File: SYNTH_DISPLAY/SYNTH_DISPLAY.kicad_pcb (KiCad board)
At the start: 2 copper layers, 51.4 x 57.8 mm, 21 parts, among them CON1 AVR-ISP-6, J1 Barrel_Jack, J2 Audio-Jack-3, SW1 SW_Push_Dual, U1 L7805, U2 MSGEQ7, U3 ATTINY85-20PU

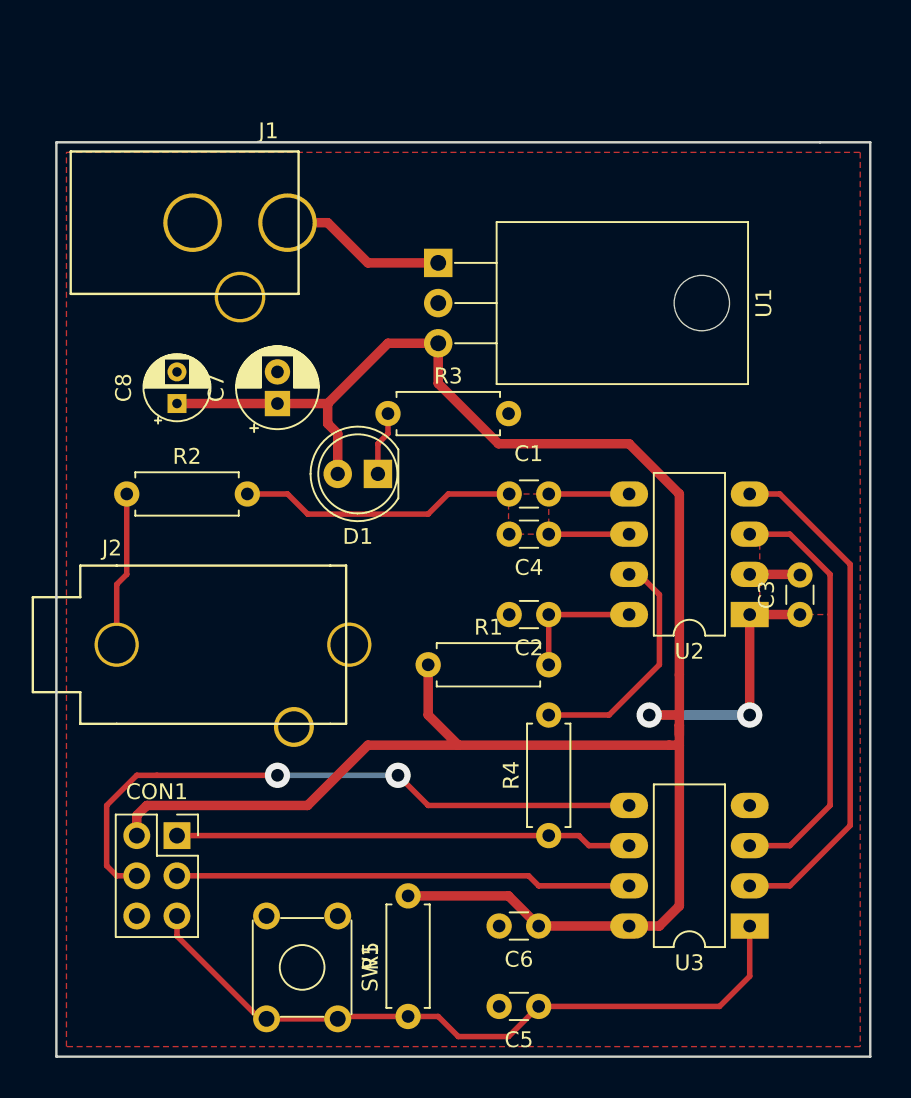
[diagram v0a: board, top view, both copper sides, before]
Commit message: added display header, mounting holes, and moved connectors
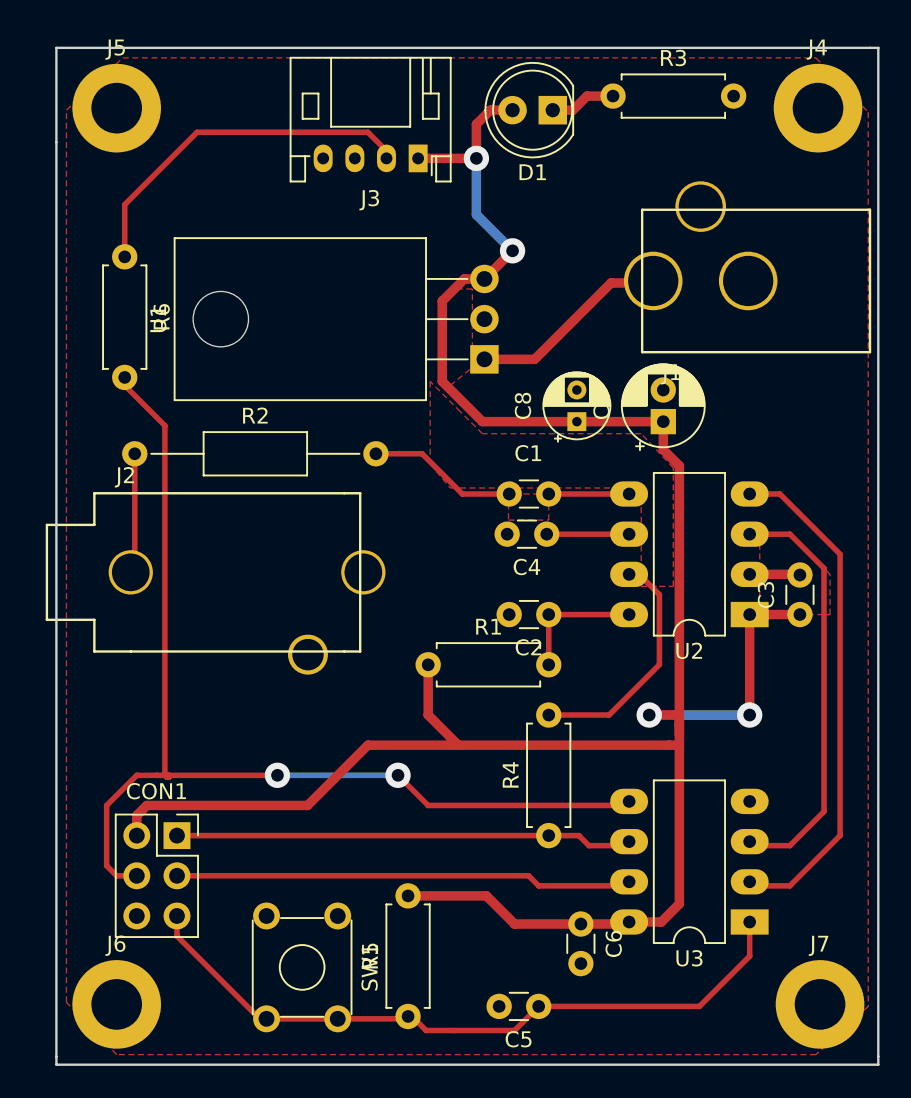
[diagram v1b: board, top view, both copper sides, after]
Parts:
- added J3: Conn_01x04, Connector_JST:JST_PH_S4B-PH-K_1x04_P2.00mm_Horizontal, F.Cu at (163.8, 64.5)
- added J4: Conn_01x01, MountingHole:MountingHole_3.2mm_M3_DIN965_Pad, F.Cu at (189.1, 61.3)
- added J5: Conn_01x01, MountingHole:MountingHole_3.2mm_M3_DIN965_Pad, F.Cu at (144.8, 61.3)
- added J6: Conn_01x01, MountingHole:MountingHole_3.2mm_M3_DIN965_Pad, F.Cu at (144.8, 118.0)
- added J7: Conn_01x01, MountingHole:MountingHole_3.2mm_M3_DIN965_Pad, F.Cu at (189.2, 118.0)
- added R6: 4.7k, Resistor_THT:R_Axial_DIN0207_L6.3mm_D2.5mm_P7.62mm_Horizontal, F.Cu at (145.3, 70.7)
- R2: footprint Resistor_THT:R_Axial_DIN0207_L6.3mm_D2.5mm_P7.62mm_Horizontal -> Resistor_THT:R_Axial_DIN0207_L6.3mm_D2.5mm_P15.24mm_Horizontal
- moved D1 25.5 mm to (172.3, 61.5)
- moved C8 25.3 mm to (173.9, 81.2)
- moved R3 24.6 mm to (176.1, 60.6)
- moved C7 24.4 mm to (179.3, 81.2)
- moved J1 23.4 mm to (178.7, 72.3), turned to 0 degrees
- moved U1 6.76 mm to (168.0, 77.2), turned to 90 degrees
- moved J2 4.66 mm to (145.7, 90.7)
- moved C6 2.67 mm to (174.1, 112.9), turned to 270 degrees
- moved R2 2.59 mm to (145.9, 83.2)
- moved U3 0.25 mm to (184.8, 112.8)
- moved C4 0.13 mm to (172.0, 88.3)
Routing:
- net /MOSI: track 39.9 -> 66.7 mm
- net /DISP: track 0.00 -> 23.0 mm
- net Net-(C1-Pad2): track 17.6 -> 9.47 mm
- net +5V: track 149.0 -> 152.9 mm, vias 2 -> 4
- net Net-(J2-Pad1): track 9.79 -> 7.60 mm
- net Net-(J1-Pad1): track 10.6 -> 12.7 mm
- net /RST: track 45.0 -> 44.1 mm
- net /STROBE: track 33.3 -> 32.7 mm
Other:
- board size 51.4 x 57.8 mm -> 51.9 x 64.3 mm
